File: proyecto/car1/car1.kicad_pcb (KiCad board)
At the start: 2 copper layers, 137.3 x 86.4 mm, 21 parts, among them J1 HC-sr04, J10 Adafruit A, J2 HC-sr04, J3 HC-sr04, J4 USB_C_Receptacle_PowerOnly_6P, J5 SERVO, J6 Adafruit A, J7 Adafruit B, J8 Conn_01x19, J9 Conn_01x19, U1 TB6612FNG

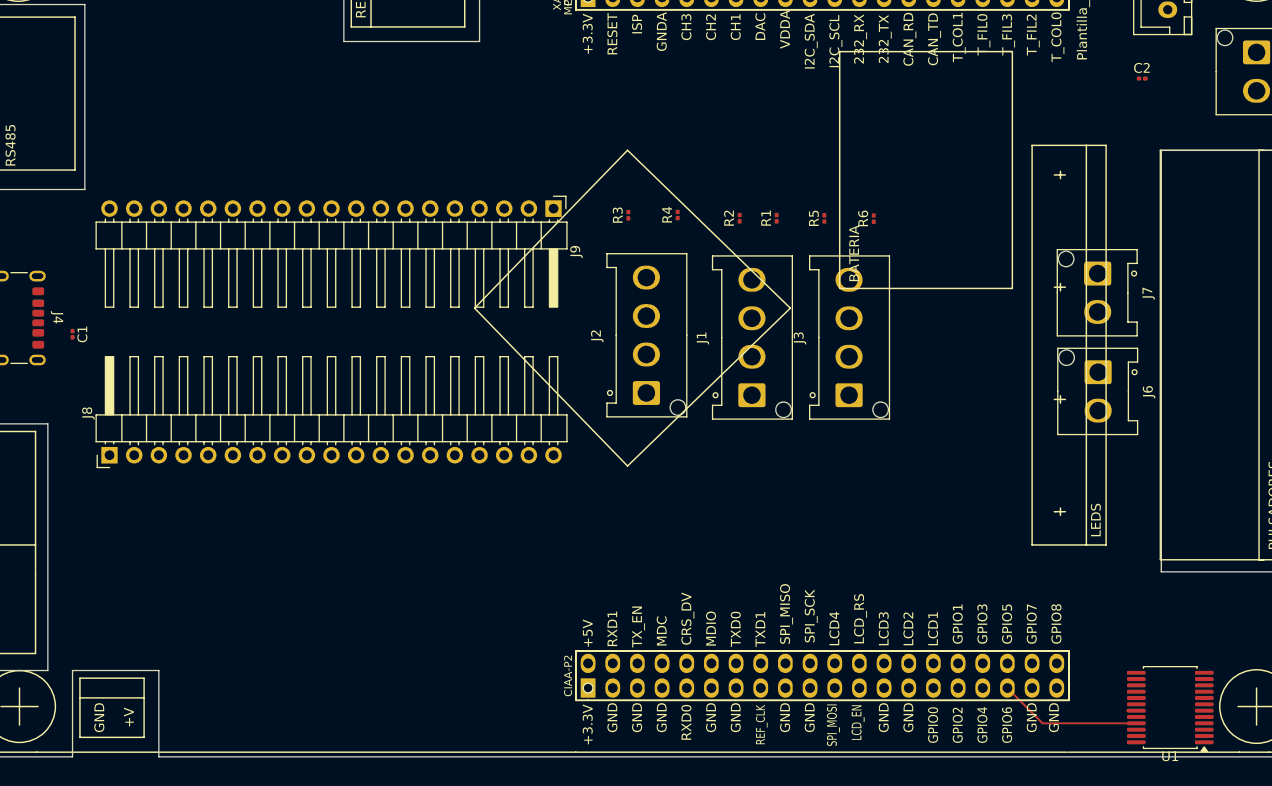
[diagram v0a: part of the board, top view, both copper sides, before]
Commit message: se agregaron los componentes
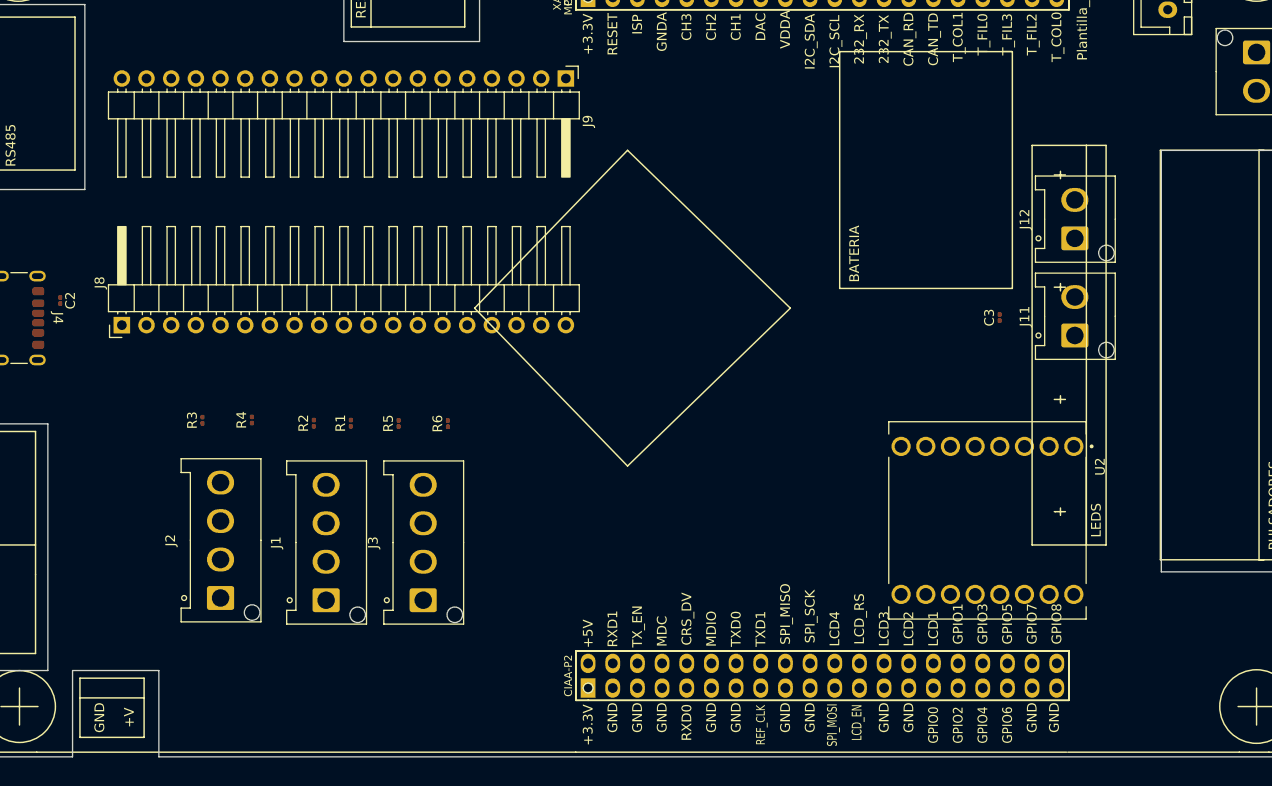
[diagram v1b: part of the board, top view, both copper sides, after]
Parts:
- removed C1: C, Capacitor_SMD:C_0201_0603Metric
- removed J6: Adafruit A, Connector_Hirose:Hirose_DF63M-2P-3.96DSA_1x02_P3.96mm_Vertical
- removed J7: Adafruit B, Connector_Hirose:Hirose_DF63M-2P-3.96DSA_1x02_P3.96mm_Vertical
- removed U1: TB6612FNG, Package_SO:SSOP-24_5.3x8.2mm_P0.65mm
- added C3: C, Capacitor_SMD:C_0201_0603Metric, F.Cu at (193.2, 88.1)
- added J11: Adafruit A, Connector_Hirose:Hirose_DF63M-2P-3.96DSA_1x02_P3.96mm_Vertical, F.Cu at (201.0, 90.0)
- added J12: Adafruit B, Connector_Hirose:Hirose_DF63M-2P-3.96DSA_1x02_P3.96mm_Vertical, F.Cu at (201.0, 80.0)
- added U2: ROB-14450, ROB-14450:MODULE_ROB-14450, F.Cu at (192.0, 109.0)
- moved C2 113.7 mm to (96.5, 86.4), turned to -90 degrees
- moved R3 48.7 mm to (111.2, 98.7)
- moved J1 48.7 mm to (123.9, 117.2)
- moved J2 48.7 mm to (113.0, 117.0)
- moved J3 48.7 mm to (133.9, 117.2)
- moved R1 48.7 mm to (126.4, 99.0)
- moved R2 48.7 mm to (122.6, 99.0)
- moved R4 48.7 mm to (116.2, 98.7)
- moved R5 48.7 mm to (131.4, 99.0)
- moved R6 48.7 mm to (136.4, 99.0)
- moved J8 13.5 mm to (102.9, 88.9)
- moved J9 13.5 mm to (148.6, 63.5)
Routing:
- net GPIO6 AIN1: track 14.8 -> 0.00 mm
- net GPIO4 STBY: track 0.95 -> 0.00 mm

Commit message: se agregaron todos los componentes
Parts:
- removed C3: C, Capacitor_SMD:C_0201_0603Metric
- removed U2: ROB-14450, ROB-14450:MODULE_ROB-14450
- added C1: C, Capacitor_SMD:C_1206_3216Metric_Pad1.33x1.80mm_HandSolder, B.Cu at (189.0, 70.3)
- added J6: Conn_01x08_Socket, Connector_PinSocket_2.54mm:PinSocket_1x08_P2.54mm_Vertical, F.Cu at (199.1, 109.7)
- added J7: Conn_01x08_Socket, Connector_PinSocket_2.54mm:PinSocket_1x08_P2.54mm_Vertical, F.Cu at (183.9, 109.7)
- C2: footprint Capacitor_SMD:C_0201_0603Metric -> Capacitor_SMD:C_1206_3216Metric_Pad1.33x1.80mm_HandSolder; moved to B.Cu
- J1, J2, J3: footprint Connector_Hirose:Hirose_DF63M-4P-3.96DSA_1x04_P3.96mm_Vertical -> Connector_Molex:Molex_KK-254_AE-6410-04A_1x04_P2.54mm_Vertical
- J10: value Adafruit A -> vcc para edu ciaa; footprint Connector_Hirose:Hirose_DF63M-2P-3.96DSA_1x02_P3.96mm_Vertical -> Connector_Molex:Molex_KK-254_AE-6410-02A_1x02_P2.54mm_Vertical
- J11, J12: footprint Connector_Hirose:Hirose_DF63M-2P-3.96DSA_1x02_P3.96mm_Vertical -> Connector_Molex:Molex_KK-254_AE-6410-02A_1x02_P2.54mm_Vertical
- J4: value USB_C_Receptacle_PowerOnly_6P -> usb c socket; footprint Connector_USB:USB_C_Receptacle_GCT_USB4125-xx-x-0190_6P_TopMnt_Horizontal -> Connector_PinSocket_2.54mm:PinSocket_2x06_P2.54mm_Vertical
- J5: footprint Connector_JST:JST_XH_B3B-XH-A_1x03_P2.50mm_Vertical -> Connector_Molex:Molex_KK-254_AE-6410-03A_1x03_P2.54mm_Vertical
- J8, J9: footprint Connector_PinHeader_2.54mm:PinHeader_1x19_P2.54mm_Horizontal -> Connector_PinSocket_2.54mm:PinSocket_1x19_P2.54mm_Vertical
- R1, R2, R3, R4, R5, R6: footprint Resistor_SMD:R_0201_0603Metric -> Resistor_SMD:R_1206_3216Metric_Pad1.30x1.75mm_HandSolder; moved to B.Cu
- moved MP? 283.9 mm to (429.5, 0.76)
- moved J10 107.2 mm to (134.6, 126.0), turned to 180 degrees
- moved R3 25.3 mm to (136.4, 98.7)
- moved R6 25.3 mm to (111.2, 99.0)
- moved R4 15.1 mm to (131.4, 98.7)
- moved R5 15.1 mm to (116.2, 99.0)
- moved J11 13.8 mm to (201.2, 76.2)
- moved J4 6.68 mm to (96.3, 83.8), turned to 0 degrees
- moved C2 6.12 mm to (101.3, 90.1)
- moved J9 5.86 mm to (154.4, 63.0)
- moved J8 5.86 mm to (108.7, 88.4)
- moved R1 5.27 mm to (121.2, 99.0)
- moved J5 3.43 mm to (207.3, 52.6), turned to 0 degrees
- moved J12 3.36 mm to (201.2, 83.3)
- moved R2 2.35 mm to (125.0, 99.0)
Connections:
- J11 pad 1: Net-(J11-Pin_1) -> A02
- J11 pad 2: Net-(J11-Pin_2) -> A01
- J12 pad 1: Net-(J12-Pin_1) -> B01
- J12 pad 2: Net-(J12-Pin_2) -> B02
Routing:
- net vcc: track 0.00 -> 127.5 mm
- net GPIO0 BIN2: track 0.00 -> 52.3 mm
- net GPIO2 BIN1: track 0.00 -> 45.1 mm
- net GPIO4 STBY: track 0.00 -> 37.9 mm
- net GPIO6 AIN1: track 0.00 -> 30.7 mm
- net GPIO8 AIN2: track 0.00 -> 18.5 mm
- added copper zone on B.Cu, net GND
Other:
- board size 137.3 x 86.4 mm -> 137.2 x 86.4 mm
- board text added: "CAN_TD"

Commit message: creacion de conexiones
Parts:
- removed MP?: Plantilla_EDU-CIAA, Poncho_Esqueleto:Plantilla_EDU-CIAA
- added R10: 0, Resistor_THT:R_Axial_DIN0207_L6.3mm_D2.5mm_P10.16mm_Horizontal, F.Cu at (192.0, 101.1)
- added R11: 0, Resistor_THT:R_Axial_DIN0207_L6.3mm_D2.5mm_P10.16mm_Horizontal, F.Cu at (152.4, 85.2)
- added R7: 0, Resistor_THT:R_Axial_DIN0207_L6.3mm_D2.5mm_P10.16mm_Horizontal, F.Cu at (195.3, 90.9)
- added R8: 0, Resistor_THT:R_Axial_DIN0207_L6.3mm_D2.5mm_P10.16mm_Horizontal, F.Cu at (170.7, 101.1)
- added R9: 0, Resistor_THT:R_Axial_DIN0207_L6.3mm_D2.5mm_P10.16mm_Horizontal, F.Cu at (180.8, 101.1)
- added REF**: MountingHole_3.2mm_M3, MountingHole:MountingHole_3.2mm_M3, F.Cu at (92.2, 51.9)
- added REF**: MountingHole_3.2mm_M3, MountingHole:MountingHole_3.2mm_M3, F.Cu at (219.7, 51.8)
- added REF**: MountingHole_3.2mm_M3, MountingHole:MountingHole_3.2mm_M3, F.Cu at (219.7, 128.2)
- J10: value vcc para edu ciaa -> vcc Edu ciaa
- moved R6 82.3 mm to (191.3, 80.2)
- moved R5 74.6 mm to (188.5, 80.2)
- moved R1 63.0 mm to (181.4, 80.2)
- moved J2 57.6 mm to (165.6, 93.5)
- moved J3 57.2 mm to (185.9, 93.5)
- moved J1 57.1 mm to (175.8, 93.5)
- moved R2 56.3 mm to (178.1, 80.2)
- moved R4 43.3 mm to (170.4, 80.0)
- moved R3 36.1 mm to (167.3, 80.0)
- moved J7 31.3 mm to (198.9, 82.3), turned to 90 degrees
- moved J11 22.5 mm to (219.3, 63.0), turned to -90 degrees
- moved J12 22.0 mm to (219.3, 70.9), turned to -90 degrees
- moved J10 21.7 mm to (113.0, 127.7)
- moved C1 17.1 mm to (202.4, 59.9)
- moved J8 14.7 mm to (111.5, 102.8)
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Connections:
- J1 pad 2: TRIGGER 2 -> Net-(J1-trigger)
- J11 pad 1: A02 -> A01
- J11 pad 2: A01 -> A02
- J12 pad 1: B01 -> B02
- J12 pad 2: B02 -> B01
- J2 pad 2: TRIGGER 1 -> Net-(J2-trigger)
- J3 pad 2: TRIGGER 3 -> Net-(J3-trigger)
- J8 pad 19: unconnected-(J8-Pin_19-Pad19) -> vcc
- J9 pad 16: Net-(J9-Pin_16) -> unconnected-(J9-Pin_16-Pad16)
- R1 pad 2: TFIL2 -> TFIL3
- R2 pad 2: TFIL2 -> TFIL3
- R3 pad 2: TFIL3 -> TFIL0
- R4 pad 2: TFIL3 -> TFIL0
- R5 pad 2: TFIL0 -> TFIL2
- R6 pad 2: TFIL0 -> TFIL2
- XA1 pad 1: unconnected-(XA1A-+3.3V-Pad1) -> 3v3
- XA1 pad 20: unconnected-(XA1A-GND-Pad20) -> GND
- XA1 pad 22: unconnected-(XA1A-GND-Pad22) -> GND
- XA1 pad 24: unconnected-(XA1A-GND-Pad24) -> GND
- XA1 pad 26: unconnected-(XA1A-GND-Pad26) -> GND
- XA1 pad 28: unconnected-(XA1A-GND-Pad28) -> GND
- XA1 pad 30: unconnected-(XA1A-GND-Pad30) -> GND
- XA1 pad 31: TCOL1 PWMB -> Net-(XA1A-tecCOL1)
- XA1 pad 32: unconnected-(XA1A-GND-Pad32) -> GND
- XA1 pad 38: unconnected-(XA1A-GND-Pad38) -> GND
- XA1 pad 39: TCOL0 PWMA -> Net-(XA1A-tecCOL0)
- XA1 pad 40: unconnected-(XA1A-GND-Pad40) -> GND
- XA1 pad 41: Net-(J9-Pin_16) -> unconnected-(XA1B-+3.3V-Pad41)
- XA1 pad 43: unconnected-(XA1B-GND-Pad43) -> GND
- XA1 pad 45: unconnected-(XA1B-GND-Pad45) -> GND
- XA1 pad 47: unconnected-(XA1B-GND-Pad47) -> GND
- XA1 pad 51: unconnected-(XA1B-GND-Pad51) -> GND
- XA1 pad 53: unconnected-(XA1B-GND-Pad53) -> GND
- XA1 pad 57: unconnected-(XA1B-GND-Pad57) -> GND
- XA1 pad 59: unconnected-(XA1B-GND-Pad59) -> GND
- XA1 pad 65: unconnected-(XA1B-GND-Pad65) -> GND
- XA1 pad 67: unconnected-(XA1B-GND-Pad67) -> GND
- XA1 pad 72: TRIGGER 1 -> GPIO1 TRIGGER 1
- XA1 pad 74: TRIGGER 2 -> GPIO3  TRIGGER 2
- XA1 pad 76: TRIGGER 3 -> GPIO5 TRIGGER 3
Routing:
- net vcc: track 127.5 -> 266.3 mm
- net TCOL1 PWMB: track 0.00 -> 62.6 mm
- net Net-(XA1A-tecCOL1): track 0.00 -> 58.7 mm
- net D7  RS232_RX: track 0.00 -> 58.1 mm
- net D6  RS232_TX: track 0.00 -> 57.3 mm
- net TFIL0: track 0.00 -> 42.8 mm
- net Net-(XA1A-tecCOL0): track 0.00 -> 37.4 mm
- net TFIL3: track 0.00 -> 35.1 mm
- net GPIO1 TRIGGER 1: track 0.00 -> 32.3 mm
- net TFIL2: track 0.00 -> 28.5 mm
- net A01: track 0.00 -> 28.4 mm
- net GPIO3  TRIGGER 2: track 0.00 -> 27.1 mm
- net A02: track 0.00 -> 24.7 mm
- net GPIO5 TRIGGER 3: track 0.00 -> 23.5 mm
- net B02: track 0.00 -> 17.9 mm
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- added copper zone on B.Cu, net vcc
